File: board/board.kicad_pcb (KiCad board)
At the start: 2 copper layers, 28.4 x 40.1 mm, 36 parts, among them J1 Conn_01x02, J101 Conn_01x06, J102 Conn_01x06, J2 Conn_01x02, J3 Conn_01x06, K1 G6K-2, K2 G6K-2, Q1 IRLB8721PBF, Q2 AO3400A, Q3 IRLB8721PBF, Q4 AO3400A, U1 ATmega8A-AU, U101 ATmega128A-AU, X101 Crystal

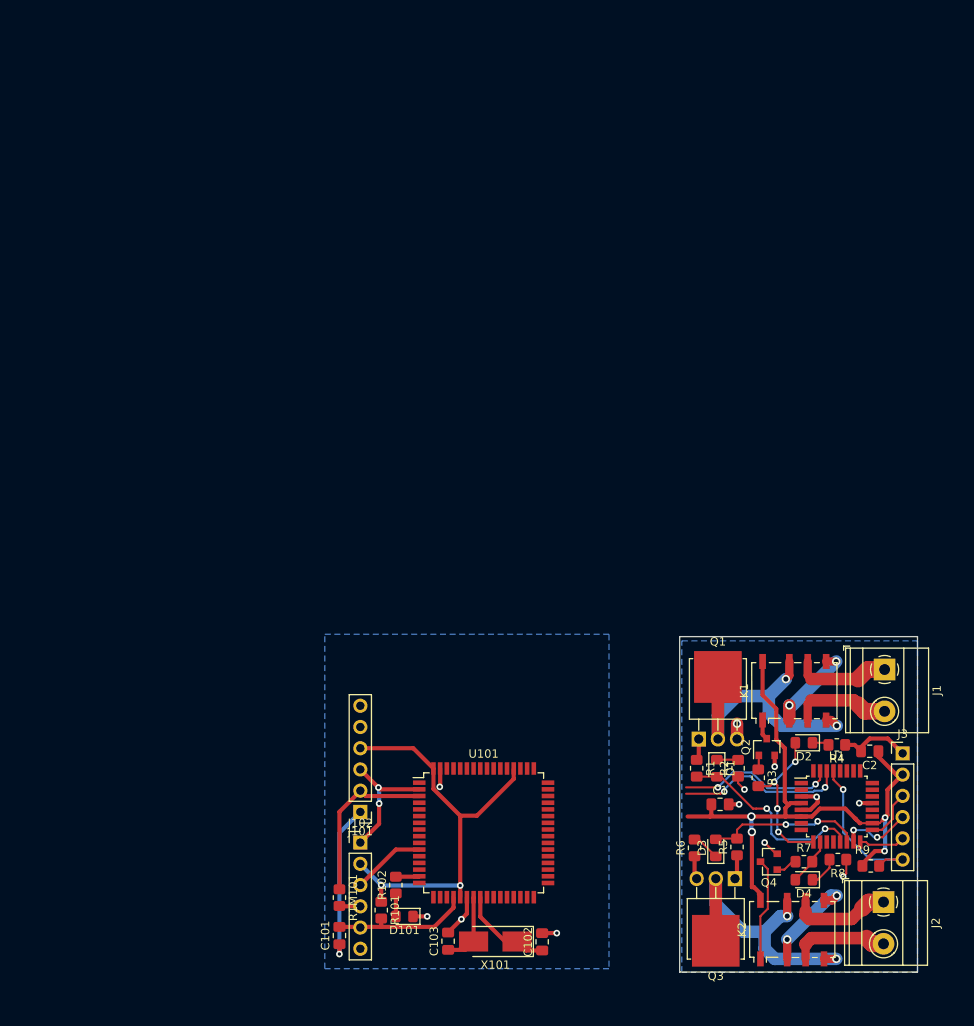
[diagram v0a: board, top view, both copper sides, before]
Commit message: uploaded updated pcb design
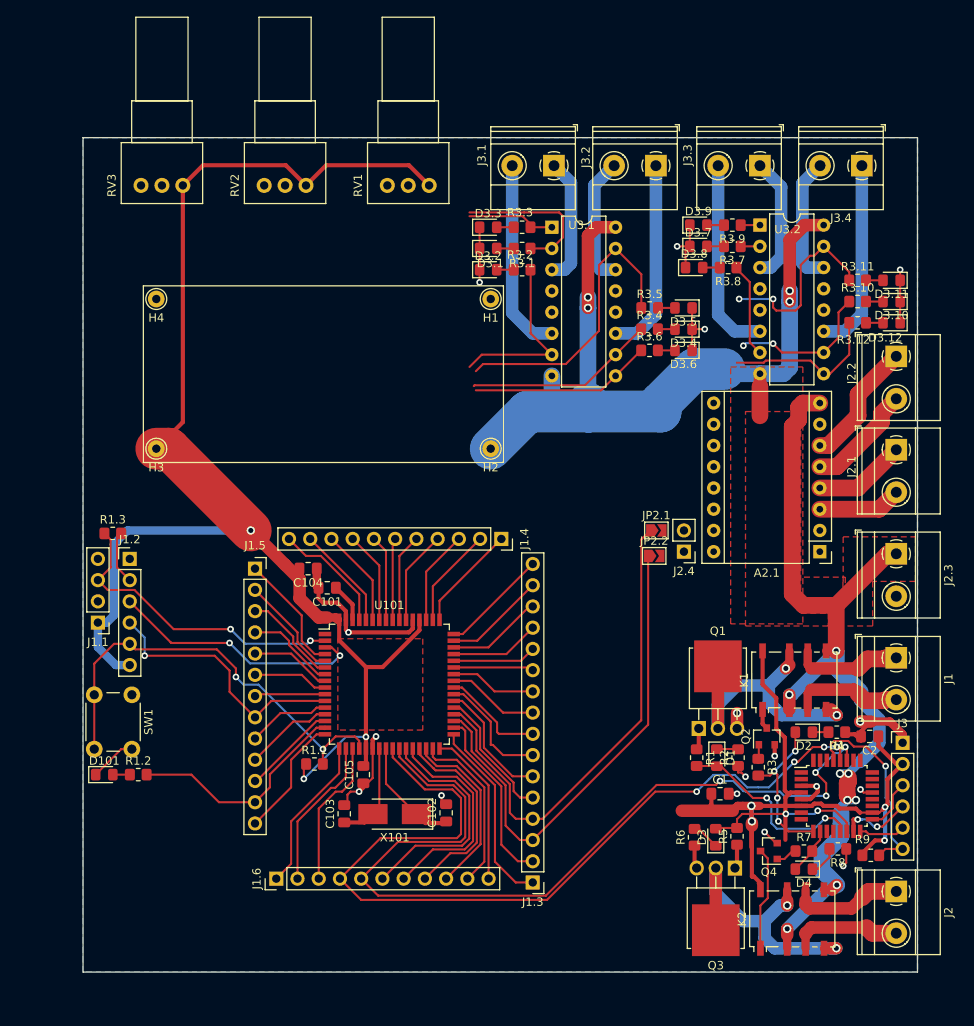
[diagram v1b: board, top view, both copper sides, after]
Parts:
- removed J101, J102: Conn_01x06, Connector_PinHeader_2.54mm:PinHeader_1x06_P2.54mm_Vertical
- removed R101, R102, R1M101: R, Resistor_SMD:R_0805_2012Metric_Pad1.20x1.40mm_HandSolder
- added A2.1: Pololu_Breakout_DRV8825, Module:Pololu_Breakout-16_15.2x20.3mm, F.Cu at (188.5, 86.9)
- added C104: C, Capacitor_SMD:C_0805_2012Metric_Pad1.18x1.45mm_HandSolder, F.Cu at (127.3, 88.9)
- added C105: C, Capacitor_SMD:C_0805_2012Metric_Pad1.18x1.45mm_HandSolder, F.Cu at (133.9, 113.5)
- added D3.1: LED, LED_SMD:LED_0805_2012Metric_Pad1.15x1.40mm_HandSolder, F.Cu at (148.8, 50.6)
- added D3.10: LED, LED_SMD:LED_0805_2012Metric_Pad1.15x1.40mm_HandSolder, F.Cu at (197.1, 56.9)
- added D3.11: LED, LED_SMD:LED_0805_2012Metric_Pad1.15x1.40mm_HandSolder, F.Cu at (197.1, 54.4)
- added D3.12: LED, LED_SMD:LED_0805_2012Metric_Pad1.15x1.40mm_HandSolder, F.Cu at (197.1, 59.5)
- added D3.2: LED, LED_SMD:LED_0805_2012Metric_Pad1.15x1.40mm_HandSolder, F.Cu at (148.8, 53.1)
- added D3.3: LED, LED_SMD:LED_0805_2012Metric_Pad1.15x1.40mm_HandSolder, F.Cu at (148.8, 48.1)
- added D3.4: LED, LED_SMD:LED_0805_2012Metric_Pad1.15x1.40mm_HandSolder, F.Cu at (172.2, 60.2)
- added D3.5: LED, LED_SMD:LED_0805_2012Metric_Pad1.15x1.40mm_HandSolder, F.Cu at (172.2, 57.7)
- added D3.6: LED, LED_SMD:LED_0805_2012Metric_Pad1.15x1.40mm_HandSolder, F.Cu at (172.2, 62.8)
- added D3.7: LED, LED_SMD:LED_0805_2012Metric_Pad1.15x1.40mm_HandSolder, F.Cu at (173.9, 50.3)
- added D3.8: LED, LED_SMD:LED_0805_2012Metric_Pad1.15x1.40mm_HandSolder, F.Cu at (173.4, 52.9)
- added D3.9: LED, LED_SMD:LED_0805_2012Metric_Pad1.15x1.40mm_HandSolder, F.Cu at (173.9, 47.8)
- added H1: GND, Connector_Pin:Pin_D1.0mm_L10.0mm, F.Cu at (149.1, 56.6)
- added H2: IN+, Connector_Pin:Pin_D1.0mm_L10.0mm, F.Cu at (149.1, 74.5)
- added H3: OUT+, Connector_Pin:Pin_D1.0mm_L10.0mm, F.Cu at (109.1, 74.5)
- added H4: GND, Connector_Pin:Pin_D1.0mm_L10.0mm, F.Cu at (109.1, 56.6)
- added J1.1: Conn_01x04, Connector_PinHeader_2.54mm:PinHeader_1x04_P2.54mm_Vertical, F.Cu at (102.1, 95.4)
- added J1.2: Conn_01x06, Connector_PinHeader_2.54mm:PinHeader_1x06_P2.54mm_Vertical, F.Cu at (105.9, 87.7)
- added J1.3: Conn_01x16, Connector_PinHeader_2.54mm:PinHeader_1x16_P2.54mm_Vertical, F.Cu at (154.1, 126.4)
- added J1.4: Conn_01x11, Connector_PinSocket_2.54mm:PinSocket_1x11_P2.54mm_Vertical, F.Cu at (150.4, 85.3)
- added J1.5: Conn_01x13, Connector_PinSocket_2.54mm:PinSocket_1x13_P2.54mm_Vertical, F.Cu at (120.9, 88.9)
- added J1.6: Conn_01x11, Connector_PinHeader_2.54mm:PinHeader_1x11_P2.54mm_Vertical, F.Cu at (123.4, 126.0)
- added J2.1: Conn_01x02, TerminalBlock_Phoenix:TerminalBlock_Phoenix_MKDS-1,5-2-5.08_1x02_P5.08mm_Horizontal, F.Cu at (197.6, 74.7)
- added J2.2: Conn_01x02, TerminalBlock_Phoenix:TerminalBlock_Phoenix_MKDS-1,5-2-5.08_1x02_P5.08mm_Horizontal, F.Cu at (197.6, 63.5)
- added J2.3: Conn_01x02, TerminalBlock_Phoenix:TerminalBlock_Phoenix_MKDS-1,5-2-5.08_1x02_P5.08mm_Horizontal, F.Cu at (197.6, 87.1)
- added J2.4: Conn_01x02, Connector_PinHeader_2.54mm:PinHeader_1x02_P2.54mm_Vertical, F.Cu at (172.2, 86.9)
- added J3.1: Conn_01x02, TerminalBlock_Phoenix:TerminalBlock_Phoenix_MKDS-1,5-2_1x02_P5.00mm_Horizontal, F.Cu at (156.7, 40.7)
- added J3.2: Conn_01x02, TerminalBlock_Phoenix:TerminalBlock_Phoenix_MKDS-1,5-2_1x02_P5.00mm_Horizontal, F.Cu at (168.9, 40.7)
- added J3.3: Conn_01x02, TerminalBlock_Phoenix:TerminalBlock_Phoenix_MKDS-1,5-2_1x02_P5.00mm_Horizontal, F.Cu at (181.3, 40.7)
- added J3.4: Conn_01x02, TerminalBlock_Phoenix:TerminalBlock_Phoenix_MKDS-1,5-2_1x02_P5.00mm_Horizontal, F.Cu at (193.5, 40.7)
- added JP2.1: Jumper_2_Open, Jumper:SolderJumper-2_P1.3mm_Open_TrianglePad1.0x1.5mm, F.Cu at (168.9, 84.3)
- added JP2.2: Jumper_2_Open, Jumper:SolderJumper-2_P1.3mm_Open_TrianglePad1.0x1.5mm, F.Cu at (168.7, 87.4)
- added R1.1: R, Resistor_SMD:R_0805_2012Metric_Pad1.20x1.40mm_HandSolder, F.Cu at (128.0, 112.3)
- added R1.2: R, Resistor_SMD:R_0805_2012Metric_Pad1.20x1.40mm_HandSolder, F.Cu at (106.9, 113.5)
- added R1.3: R, Resistor_SMD:R_0805_2012Metric_Pad1.20x1.40mm_HandSolder, F.Cu at (103.9, 84.7)
- added R3.1: 200, Resistor_SMD:R_0805_2012Metric_Pad1.20x1.40mm_HandSolder, F.Cu at (152.9, 50.6)
- added R3.10: 200, Resistor_SMD:R_0805_2012Metric_Pad1.20x1.40mm_HandSolder, F.Cu at (193.0, 56.9)
- added R3.11: 200, Resistor_SMD:R_0805_2012Metric_Pad1.20x1.40mm_HandSolder, F.Cu at (193.0, 54.4)
- added R3.12: 200, Resistor_SMD:R_0805_2012Metric_Pad1.20x1.40mm_HandSolder, F.Cu at (193.0, 59.5)
- added R3.2: 200, Resistor_SMD:R_0805_2012Metric_Pad1.20x1.40mm_HandSolder, F.Cu at (152.9, 53.1)
- added R3.3: 200, Resistor_SMD:R_0805_2012Metric_Pad1.20x1.40mm_HandSolder, F.Cu at (152.9, 48.1)
- added R3.4: 200, Resistor_SMD:R_0805_2012Metric_Pad1.20x1.40mm_HandSolder, F.Cu at (168.1, 60.2)
- added R3.5: 200, Resistor_SMD:R_0805_2012Metric_Pad1.20x1.40mm_HandSolder, F.Cu at (168.1, 57.7)
- added R3.6: 200, Resistor_SMD:R_0805_2012Metric_Pad1.20x1.40mm_HandSolder, F.Cu at (168.1, 62.8)
- added R3.7: 200, Resistor_SMD:R_0805_2012Metric_Pad1.20x1.40mm_HandSolder, F.Cu at (178.0, 50.3)
- added R3.8: 200, Resistor_SMD:R_0805_2012Metric_Pad1.20x1.40mm_HandSolder, F.Cu at (177.5, 52.9)
- added R3.9: 200, Resistor_SMD:R_0805_2012Metric_Pad1.20x1.40mm_HandSolder, F.Cu at (178.0, 47.8)
- added RV1: R_POT, Potentiometer_THT:Potentiometer_Alps_RK097_Single_Horizontal, F.Cu at (141.7, 43.1)
- added RV2: R_POT, Potentiometer_THT:Potentiometer_Alps_RK097_Single_Horizontal, F.Cu at (127.0, 43.1)
- added RV3: R_POT, Potentiometer_THT:Potentiometer_Alps_RK097_Single_Horizontal, F.Cu at (112.3, 43.1)
- added SW1: SW_Push, Button_Switch_THT:SW_PUSH_6mm_H4.3mm, F.Cu at (106.2, 104.0)
- added U3.1: L293D, Package_DIP:DIP-16_W7.62mm, F.Cu at (156.4, 48.1)
- added U3.2: L293D, Package_DIP:DIP-16_W7.62mm, F.Cu at (181.3, 47.8)
- moved C101 41.6 mm to (129.5, 91.2), turned to 180 degrees
- moved D101 39.7 mm to (102.9, 113.5), turned to 0 degrees
- moved U101 21.1 mm to (137.0, 102.7)
- moved C103 19.7 mm to (131.6, 118.2)
- moved X101 19.4 mm to (137.6, 118.3)
- moved C102 19.2 mm to (143.8, 118.1)
- moved J2 1.98 mm to (197.6, 127.5)
- moved J1 1.98 mm to (197.6, 99.6)
- moved C2 1.78 mm to (194.4, 109.0)
- moved R4 1.52 mm to (190.5, 108.5)
- moved D4 1.27 mm to (186.6, 124.8)
- moved J3 1.27 mm to (198.4, 109.7)
- moved K2 1.27 mm to (185.2, 130.8)
- moved Q1 1.27 mm to (174.0, 108.0)
- moved Q2 1.27 mm to (182.1, 109.0)
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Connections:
- net /RX renamed Net-(U1-Pad30)
- net /TX renamed Net-(U1-Pad31)
- net /V_MOT renamed V_MOT
- C1 pad 1: /5V -> 5V
- C101 pad 1: /Sheet5F90A712/DTR -> Net-(C101-Pad1)
- C101 pad 2: /Sheet5F90A712/RESET -> GND
- C2 pad 1: /5V -> 5V
- J3 pad 2: /5V -> 5V
- K1 pad 8: /5V -> 5V
- K2 pad 8: /5V -> 5V
- R9 pad 2: /5V -> 5V
- U1 pad 18: /5V -> 5V
- U1 pad 27: Net-(U1-Pad27) -> PD1
- U1 pad 28: Net-(U1-Pad28) -> PD0
- U1 pad 4: /5V -> 5V
- U1 pad 6: /5V -> 5V
- U101 pad 10: Net-(U101-Pad10) -> PB0
- U101 pad 11: /Sheet5F90A712/SCK -> PB1
- U101 pad 12: Net-(U101-Pad12) -> PB2
- U101 pad 13: Net-(U101-Pad13) -> PB3
- U101 pad 14: Net-(U101-Pad14) -> PB4
- U101 pad 15: Net-(R102-Pad2) -> PB5
- U101 pad 16: Net-(U101-Pad16) -> PB6
- U101 pad 17: Net-(U101-Pad17) -> PB7
- U101 pad 18: Net-(U101-Pad18) -> PG3
- U101 pad 19: Net-(U101-Pad19) -> PG4
- U101 pad 2: /Sheet5F90A712/TX -> /atmega128/TX
- U101 pad 20: /Sheet5F90A712/RESET -> /atmega128/RESET
- U101 pad 21: VCC -> 5V
- U101 pad 25: Net-(U101-Pad25) -> PD0
- U101 pad 26: Net-(U101-Pad26) -> PD1
- U101 pad 27: Net-(U101-Pad27) -> PD2
- U101 pad 28: Net-(U101-Pad28) -> PD3
- U101 pad 29: Net-(U101-Pad29) -> PD4
- U101 pad 3: /Sheet5F90A712/RX -> /atmega128/PDO
- U101 pad 30: Net-(U101-Pad30) -> PD5
- U101 pad 31: Net-(U101-Pad31) -> PD6
- U101 pad 32: Net-(U101-Pad32) -> PD7
- U101 pad 33: Net-(U101-Pad33) -> PG0
- U101 pad 34: Net-(U101-Pad34) -> PG1
- U101 pad 35: Net-(U101-Pad35) -> PC0
- U101 pad 36: Net-(U101-Pad36) -> PC1
- U101 pad 37: Net-(U101-Pad37) -> PC2
- U101 pad 38: Net-(U101-Pad38) -> PC3
- U101 pad 39: Net-(U101-Pad39) -> PC4
- U101 pad 4: Net-(U101-Pad4) -> PE2
- U101 pad 40: Net-(U101-Pad40) -> PC5
- U101 pad 41: Net-(U101-Pad41) -> PC6
- U101 pad 42: Net-(U101-Pad42) -> PC7
- U101 pad 43: Net-(U101-Pad43) -> PG2
- U101 pad 44: Net-(U101-Pad44) -> PA7
- U101 pad 45: Net-(U101-Pad45) -> PA6
- U101 pad 46: Net-(U101-Pad46) -> PA5
- U101 pad 47: Net-(U101-Pad47) -> PA4
- U101 pad 48: Net-(U101-Pad48) -> PA3
- U101 pad 49: Net-(U101-Pad49) -> PA2
- U101 pad 5: Net-(U101-Pad5) -> M1PWM
- U101 pad 50: Net-(U101-Pad50) -> PA1
- U101 pad 51: Net-(U101-Pad51) -> PA0
- U101 pad 52: VCC -> 5V
- U101 pad 54: Net-(U101-Pad54) -> PF7
- U101 pad 55: Net-(U101-Pad55) -> PF6
- U101 pad 56: Net-(U101-Pad56) -> PF5
- U101 pad 57: Net-(U101-Pad57) -> PF4
- U101 pad 58: Net-(U101-Pad58) -> PF3
- U101 pad 59: Net-(U101-Pad59) -> PF2
- U101 pad 6: Net-(U101-Pad6) -> PE4
- U101 pad 60: Net-(U101-Pad60) -> PF1
- U101 pad 61: Net-(U101-Pad61) -> PF0
- U101 pad 62: Net-(U101-Pad62) -> Net-(C101-Pad1)
- U101 pad 64: VCC -> 5V
- U101 pad 7: Net-(U101-Pad7) -> PE5
- U101 pad 8: Net-(U101-Pad8) -> PE6
- U101 pad 9: Net-(U101-Pad9) -> PE7
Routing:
- net 5V: track 0.00 -> 260.5 mm, vias 0 -> 7
- net V_MOT: track 22.9 -> 199.5 mm, vias 4 -> 12
- net PD0: track 0.00 -> 103.6 mm, vias 0 -> 4
- net PD1: track 0.00 -> 103.1 mm, vias 0 -> 4
- net /5V: track 77.6 -> 0.00 mm, vias 4 -> 0
- net PC0: track 0.00 -> 59.2 mm
- net PC1: track 0.00 -> 59.1 mm
- net GND: track 39.8 -> 95.4 mm, vias 12 -> 17
- net /atmega128/RESET: track 0.00 -> 52.3 mm, vias 0 -> 2
- net VCC: track 51.0 -> 0.00 mm, vias 2 -> 0
- net /atmega128/TX: track 0.00 -> 37.2 mm, vias 0 -> 2
- net M2B: track 0.00 -> 35.8 mm
- net PB1: track 0.00 -> 31.6 mm, vias 0 -> 1
- net /atmega128/PDO: track 0.00 -> 30.8 mm, vias 0 -> 2
- net PD2: track 0.00 -> 28.1 mm
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- added copper zone on F.Cu, net 5V
- added copper zone on F.Cu, net V_MOT
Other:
- board size 28.4 x 40.1 mm -> 99.8 x 99.8 mm

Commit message: updated pcb design
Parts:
- added D1.2: LED, LED_SMD:LED_0805_2012Metric_Pad1.15x1.40mm_HandSolder, F.Cu at (110.7, 90.2)
- added D1.3: LED, LED_SMD:LED_0805_2012Metric_Pad1.15x1.40mm_HandSolder, F.Cu at (110.5, 94.0)
- added D1.4: LED, LED_SMD:LED_0805_2012Metric_Pad1.15x1.40mm_HandSolder, F.Cu at (110.6, 98.1)
- added D1.5: LED, LED_SMD:LED_0805_2012Metric_Pad1.15x1.40mm_HandSolder, F.Cu at (110.5, 102.4)
- added H5: MountingHole, MountingHole:MountingHole_2.5mm_Pad, F.Cu at (103.8, 50.4)
- added H6: MountingHole, MountingHole:MountingHole_2.5mm_Pad, F.Cu at (103.7, 125.7)
- added H7: MountingHole, MountingHole:MountingHole_2.5mm_Pad, F.Cu at (168.3, 76.3)
- added J1.11: EN, TestPoint:TestPoint_THTPad_1.0x1.0mm_Drill0.5mm, F.Cu at (156.2, 117.8)
- added J1.12: ALED, TestPoint:TestPoint_THTPad_1.0x1.0mm_Drill0.5mm, F.Cu at (156.2, 119.3)
- added J1.13: STAT, TestPoint:TestPoint_THTPad_1.0x1.0mm_Drill0.5mm, F.Cu at (156.2, 120.8)
- added J1.14: SELECT, TestPoint:TestPoint_THTPad_1.0x1.0mm_Drill0.5mm, F.Cu at (156.2, 122.3)
- added J1.15: , TestPoint:TestPoint_THTPad_1.0x1.0mm_Drill0.5mm, F.Cu at (156.2, 123.8)
- added J1.16: , TestPoint:TestPoint_THTPad_1.0x1.0mm_Drill0.5mm, F.Cu at (156.2, 125.3)
- added J1.17: , TestPoint:TestPoint_THTPad_1.0x1.0mm_Drill0.5mm, F.Cu at (156.2, 126.8)
- added J1.18: , TestPoint:TestPoint_THTPad_1.0x1.0mm_Drill0.5mm, F.Cu at (156.2, 128.3)
- added J1.19: , TestPoint:TestPoint_THTPad_1.0x1.0mm_Drill0.5mm, F.Cu at (156.2, 129.8)
- added J1.20: , TestPoint:TestPoint_THTPad_1.0x1.0mm_Drill0.5mm, F.Cu at (156.2, 131.3)
- added J1.21: , TestPoint:TestPoint_THTPad_1.0x1.0mm_Drill0.5mm, F.Cu at (156.2, 132.8)
- added J1.22: , TestPoint:TestPoint_THTPad_1.0x1.0mm_Drill0.5mm, F.Cu at (156.2, 134.3)
- added J1.23: GND, TestPoint:TestPoint_THTPad_1.0x1.0mm_Drill0.5mm, F.Cu at (169.9, 116.2)
- added J1.24: VCC, TestPoint:TestPoint_THTPad_1.0x1.0mm_Drill0.5mm, F.Cu at (169.9, 117.7)
- added J1.25: RST, TestPoint:TestPoint_THTPad_1.0x1.0mm_Drill0.5mm, F.Cu at (169.9, 119.2)
- added J1.26: , TestPoint:TestPoint_THTPad_1.0x1.0mm_Drill0.5mm, F.Cu at (169.9, 120.7)
- added J1.27: SWI, TestPoint:TestPoint_THTPad_1.0x1.0mm_Drill0.5mm, F.Cu at (169.9, 122.2)
- added J1.28: , TestPoint:TestPoint_THTPad_1.0x1.0mm_Drill0.5mm, F.Cu at (169.9, 123.7)
- added J1.29: , TestPoint:TestPoint_THTPad_1.0x1.0mm_Drill0.5mm, F.Cu at (169.9, 125.2)
- added J1.30: , TestPoint:TestPoint_THTPad_1.0x1.0mm_Drill0.5mm, F.Cu at (169.9, 126.7)
- added J1.31: , TestPoint:TestPoint_THTPad_1.0x1.0mm_Drill0.5mm, F.Cu at (169.9, 128.2)
- added J1.32: RTS, TestPoint:TestPoint_THTPad_1.0x1.0mm_Drill0.5mm, F.Cu at (169.9, 129.7)
- added J1.33: CTS, TestPoint:TestPoint_THTPad_1.0x1.0mm_Drill0.5mm, F.Cu at (169.9, 131.2)
- added J1.34: RXD, TestPoint:TestPoint_THTPad_1.0x1.0mm_Drill0.5mm, F.Cu at (169.9, 132.7)
- added J1.35: TXD, TestPoint:TestPoint_THTPad_1.0x1.0mm_Drill0.5mm, F.Cu at (169.9, 134.2)
- added J1.36: Conn_01x04, Connector_PinHeader_2.54mm:PinHeader_1x04_P2.54mm_Vertical, F.Cu at (105.8, 112.3)
- added J1.7: Conn_01x04, Connector_PinHeader_2.54mm:PinHeader_1x04_P2.54mm_Vertical, F.Cu at (115.8, 119.4)
- added J2.5: Conn_01x04, Connector_PinHeader_2.54mm:PinHeader_1x04_P2.54mm_Vertical, F.Cu at (101.8, 56.0)
- added J2.6: Conn_01x04, Connector_PinHeader_2.54mm:PinHeader_1x04_P2.54mm_Vertical, F.Cu at (104.9, 55.9)
- added J2.7: Conn_01x04, Connector_PinHeader_2.54mm:PinHeader_1x04_P2.54mm_Vertical, F.Cu at (104.8, 67.9)
- added J2.8: Conn_01x04, Connector_PinHeader_2.54mm:PinHeader_1x04_P2.54mm_Vertical, F.Cu at (101.8, 67.9)
- added J3.5: Conn_01x06, Connector_PinHeader_2.54mm:PinHeader_1x06_P2.54mm_Vertical, F.Cu at (116.5, 69.1)
- added J3.6: Conn_01x06, Connector_PinHeader_2.54mm:PinHeader_1x06_P2.54mm_Vertical, F.Cu at (132.7, 69.1)
- added J37: Conn_01x05, Connector_PinHeader_2.54mm:PinHeader_1x05_P2.54mm_Vertical, F.Cu at (168.1, 115.7)
- added JP1.1: M4PWM, Jumper:SolderJumper-2_P1.3mm_Open_TrianglePad1.0x1.5mm, F.Cu at (109.3, 120.5)
- added JP1.2: M4PWM, Jumper:SolderJumper-2_P1.3mm_Open_TrianglePad1.0x1.5mm, F.Cu at (109.4, 117.7)
- added JP1.3: M4PWM, Jumper:SolderJumper-2_P1.3mm_Open_TrianglePad1.0x1.5mm, F.Cu at (109.4, 114.8)
- added JP1.4: M4PWM, Jumper:SolderJumper-2_P1.3mm_Open_TrianglePad1.0x1.5mm, F.Cu at (109.3, 112.0)
- added JP3.10: M1B, Jumper:SolderJumper-2_P1.3mm_Open_TrianglePad1.0x1.5mm, F.Cu at (116.3, 72.2)
- added JP3.11: M4PWM, Jumper:SolderJumper-2_P1.3mm_Open_TrianglePad1.0x1.5mm, F.Cu at (145.3, 72.3)
- added JP3.12: M4A, Jumper:SolderJumper-2_P1.3mm_Open_TrianglePad1.0x1.5mm, F.Cu at (142.9, 72.3)
- added JP3.13: M4B, Jumper:SolderJumper-2_P1.3mm_Open_TrianglePad1.0x1.5mm, F.Cu at (140.2, 72.2)
- added JP3.14: M3A, Jumper:SolderJumper-2_P1.3mm_Open_TrianglePad1.0x1.5mm, F.Cu at (137.7, 72.3)
- added JP3.15: M3PWM, Jumper:SolderJumper-2_P1.3mm_Open_TrianglePad1.0x1.5mm, F.Cu at (135.1, 72.3)
- added JP3.16: M3B, Jumper:SolderJumper-2_P1.3mm_Open_TrianglePad1.0x1.5mm, F.Cu at (132.6, 72.3)
- added JP3.5: M2PWM, Jumper:SolderJumper-2_P1.3mm_Open_TrianglePad1.0x1.5mm, F.Cu at (128.9, 72.3)
- added JP3.6: M2A, Jumper:SolderJumper-2_P1.3mm_Open_TrianglePad1.0x1.5mm, F.Cu at (126.5, 72.2)
- added JP3.7: M2B, Jumper:SolderJumper-2_P1.3mm_Open_TrianglePad1.0x1.5mm, F.Cu at (124.0, 72.2)
- added JP3.8: M1PWM, Jumper:SolderJumper-2_P1.3mm_Open_TrianglePad1.0x1.5mm, F.Cu at (121.4, 72.2)
- added JP3.9: M1A, Jumper:SolderJumper-2_P1.3mm_Open_TrianglePad1.0x1.5mm, F.Cu at (118.9, 72.2)
- added Q1.1: AO3400A, Package_TO_SOT_SMD:SOT-23, F.Cu at (166.1, 111.6)
- added R1.10: R, Resistor_SMD:R_0805_2012Metric_Pad1.20x1.40mm_HandSolder, F.Cu at (160.0, 124.2)
- added R1.11: R, Resistor_SMD:R_0805_2012Metric_Pad1.20x1.40mm_HandSolder, F.Cu at (163.9, 124.2)
- added R1.12: R, Resistor_SMD:R_0805_2012Metric_Pad1.20x1.40mm_HandSolder, F.Cu at (162.0, 112.5)
- added R1.13: R, Resistor_SMD:R_0805_2012Metric_Pad1.20x1.40mm_HandSolder, F.Cu at (119.9, 130.6)
- added R1.14: R, Resistor_SMD:R_0805_2012Metric_Pad1.20x1.40mm_HandSolder, F.Cu at (119.9, 132.8)
- added R1.4: R, Resistor_SMD:R_0805_2012Metric_Pad1.20x1.40mm_HandSolder, F.Cu at (113.6, 91.0)
- added R1.5: R, Resistor_SMD:R_0805_2012Metric_Pad1.20x1.40mm_HandSolder, F.Cu at (113.5, 94.9)
- added R1.6: R, Resistor_SMD:R_0805_2012Metric_Pad1.20x1.40mm_HandSolder, F.Cu at (113.5, 98.9)
- added R1.7: R, Resistor_SMD:R_0805_2012Metric_Pad1.20x1.40mm_HandSolder, F.Cu at (113.4, 102.9)
- added R1.8: R, Resistor_SMD:R_0805_2012Metric_Pad1.20x1.40mm_HandSolder, F.Cu at (166.1, 108.4)
- added R1.9: R, Resistor_SMD:R_0805_2012Metric_Pad1.20x1.40mm_HandSolder, F.Cu at (162.0, 110.1)
- added SW1.2: SW_Push, Button_Switch_THT:SW_PUSH_6mm_H4.3mm, F.Cu at (123.7, 130.5)
- added SW1.3: SW_Push, Button_Switch_THT:SW_PUSH_6mm_H4.3mm, F.Cu at (134.1, 130.5)
- added TP1: TestPoint, TestPoint:TestPoint_Pad_4.0x4.0mm, F.Cu at (169.3, 91.4)
- added TP10: TestPoint, TestPoint:TestPoint_Pad_4.0x4.0mm, B.Cu at (143.0, 58.5)
- added TP100: TestPoint, TestPoint:TestPoint_Pad_4.0x4.0mm, F.Cu at (110.3, 125.3)
- added TP101: TestPoint, TestPoint:TestPoint_Pad_4.0x4.0mm, F.Cu at (108.3, 134.1)
- added TP102: TestPoint, TestPoint:TestPoint_Pad_4.0x4.0mm, F.Cu at (110.3, 129.7)
- added TP11: TestPoint, TestPoint:TestPoint_Pad_4.0x4.0mm, B.Cu at (138.6, 58.5)
- added TP12: TestPoint, TestPoint:TestPoint_Pad_4.0x4.0mm, F.Cu at (164.5, 95.8)
- added TP13: TestPoint, TestPoint:TestPoint_Pad_4.0x4.0mm, B.Cu at (123.1, 54.1)
- added TP14: TestPoint, TestPoint:TestPoint_Pad_4.0x4.0mm, B.Cu at (140.7, 54.1)
- added TP15: TestPoint, TestPoint:TestPoint_Pad_4.0x4.0mm, B.Cu at (140.7, 62.9)
- added TP16: TestPoint, TestPoint:TestPoint_Pad_4.0x4.0mm, B.Cu at (134.2, 58.5)
- added TP17: TestPoint, TestPoint:TestPoint_Pad_4.0x4.0mm, B.Cu at (136.3, 54.1)
- added TP18: TestPoint, TestPoint:TestPoint_Pad_4.0x4.0mm, F.Cu at (160.0, 128.8)
- added TP19: TestPoint, TestPoint:TestPoint_Pad_4.0x4.0mm, B.Cu at (143.0, 49.7)
- added TP2: TestPoint, TestPoint:TestPoint_Pad_4.0x4.0mm, F.Cu at (163.2, 91.4)
- added TP20: TestPoint, TestPoint:TestPoint_Pad_4.0x4.0mm, B.Cu at (136.3, 62.9)
- added TP21: TestPoint, TestPoint:TestPoint_Pad_4.0x4.0mm, B.Cu at (169.2, 91.4)
- added TP22: TestPoint, TestPoint:TestPoint_Pad_4.0x4.0mm, B.Cu at (129.8, 58.5)
- added TP23: TestPoint, TestPoint:TestPoint_Pad_4.0x4.0mm, B.Cu at (131.9, 54.1)
- added TP24: TestPoint, TestPoint:TestPoint_Pad_4.0x4.0mm, B.Cu at (138.6, 49.7)
- added TP25: TestPoint, TestPoint:TestPoint_Pad_4.0x4.0mm, F.Cu at (160.1, 104.6)
- added TP26: TestPoint, TestPoint:TestPoint_Pad_4.0x4.0mm, B.Cu at (131.9, 62.9)
- added TP27: TestPoint, TestPoint:TestPoint_Pad_4.0x4.0mm, B.Cu at (163.2, 91.4)
- added TP28: TestPoint, TestPoint:TestPoint_Pad_4.0x4.0mm, B.Cu at (162.1, 109.0)
- added TP29: TestPoint, TestPoint:TestPoint_Pad_4.0x4.0mm, B.Cu at (125.4, 58.5)
- added TP3: TestPoint, TestPoint:TestPoint_Pad_4.0x4.0mm, F.Cu at (168.9, 104.6)
- added TP30: TestPoint, TestPoint:TestPoint_Pad_4.0x4.0mm, B.Cu at (127.5, 54.1)
- added TP31: TestPoint, TestPoint:TestPoint_Pad_4.0x4.0mm, B.Cu at (134.2, 49.7)
- added TP32: TestPoint, TestPoint:TestPoint_Pad_4.0x4.0mm, F.Cu at (116.3, 80.8)
- added TP33: TestPoint, TestPoint:TestPoint_Pad_4.0x4.0mm, B.Cu at (127.5, 62.9)
- added TP34: TestPoint, TestPoint:TestPoint_Pad_4.0x4.0mm, B.Cu at (150.9, 133.8)
- added TP35: TestPoint, TestPoint:TestPoint_Pad_4.0x4.0mm, B.Cu at (166.5, 109.0)
- added TP36: TestPoint, TestPoint:TestPoint_Pad_4.0x4.0mm, B.Cu at (168.9, 104.6)
- added TP37: TestPoint, TestPoint:TestPoint_Pad_4.0x4.0mm, F.Cu at (160.1, 95.8)
- added TP38: TestPoint, TestPoint:TestPoint_Pad_4.0x4.0mm, B.Cu at (129.8, 49.7)
- added TP39: TestPoint, TestPoint:TestPoint_Pad_4.0x4.0mm, B.Cu at (116.6, 49.7)
- added TP4: TestPoint, TestPoint:TestPoint_Pad_4.0x4.0mm, F.Cu at (160.0, 133.2)
- added TP40: TestPoint, TestPoint:TestPoint_Pad_4.0x4.0mm, B.Cu at (123.1, 62.9)
- added TP41: TestPoint, TestPoint:TestPoint_Pad_4.0x4.0mm, B.Cu at (176.2, 92.9)
- added TP42: TestPoint, TestPoint:TestPoint_Pad_4.0x4.0mm, F.Cu at (116.6, 58.5)
- added TP43: TestPoint, TestPoint:TestPoint_Pad_4.0x4.0mm, B.Cu at (164.5, 104.6)
- added TP44: TestPoint, TestPoint:TestPoint_Pad_4.0x4.0mm, B.Cu at (160.1, 104.6)
- added TP45: TestPoint, TestPoint:TestPoint_Pad_4.0x4.0mm, B.Cu at (125.4, 49.7)
- added TP46: TestPoint, TestPoint:TestPoint_Pad_4.0x4.0mm, B.Cu at (121.0, 49.7)
- added TP47: TestPoint, TestPoint:TestPoint_Pad_4.0x4.0mm, B.Cu at (118.7, 62.9)
- added TP48: TestPoint, TestPoint:TestPoint_Pad_4.0x4.0mm, B.Cu at (182.8, 88.5)
- added TP49: TestPoint, TestPoint:TestPoint_Pad_4.0x4.0mm, F.Cu at (138.6, 49.7)
- added TP5: TestPoint, TestPoint:TestPoint_Pad_4.0x4.0mm, F.Cu at (164.5, 104.6)
- added TP50: TestPoint, TestPoint:TestPoint_Pad_4.0x4.0mm, F.Cu at (136.3, 54.1)
- added TP51: TestPoint, TestPoint:TestPoint_Pad_4.0x4.0mm, B.Cu at (166.8, 100.2)
- added TP52: TestPoint, TestPoint:TestPoint_Pad_4.0x4.0mm, B.Cu at (168.9, 95.8)
- added TP53: TestPoint, TestPoint:TestPoint_Pad_4.0x4.0mm, B.Cu at (118.7, 54.1)
- added TP54: TestPoint, TestPoint:TestPoint_Pad_4.0x4.0mm, B.Cu at (146.5, 133.8)
- added TP55: TestPoint, TestPoint:TestPoint_Pad_4.0x4.0mm, B.Cu at (182.8, 84.1)
- added TP56: TestPoint, TestPoint:TestPoint_Pad_4.0x4.0mm, F.Cu at (138.6, 58.5)
- added TP57: TestPoint, TestPoint:TestPoint_Pad_4.0x4.0mm, F.Cu at (140.7, 54.1)
- added TP58: TestPoint, TestPoint:TestPoint_Pad_4.0x4.0mm, F.Cu at (143.0, 49.7)
- added TP59: TestPoint, TestPoint:TestPoint_Pad_4.0x4.0mm, B.Cu at (162.4, 100.2)
- added TP6: TestPoint, TestPoint:TestPoint_Pad_4.0x4.0mm, B.Cu at (121.0, 58.5)
- added TP60: TestPoint, TestPoint:TestPoint_Pad_4.0x4.0mm, B.Cu at (164.5, 95.8)
- added TP61: TestPoint, TestPoint:TestPoint_Pad_4.0x4.0mm, B.Cu at (108.3, 134.1)
- added TP62: TestPoint, TestPoint:TestPoint_Pad_4.0x4.0mm, B.Cu at (182.8, 79.7)
- added TP63: TestPoint, TestPoint:TestPoint_Pad_4.0x4.0mm, F.Cu at (143.0, 58.5)
- added TP64: TestPoint, TestPoint:TestPoint_Pad_4.0x4.0mm, F.Cu at (121.0, 58.5)
- added TP65: TestPoint, TestPoint:TestPoint_Pad_4.0x4.0mm, F.Cu at (123.1, 54.1)
- added TP66: TestPoint, TestPoint:TestPoint_Pad_4.0x4.0mm, F.Cu at (121.0, 49.7)
- added TP67: TestPoint, TestPoint:TestPoint_Pad_4.0x4.0mm, B.Cu at (160.1, 95.8)
- added TP68: TestPoint, TestPoint:TestPoint_Pad_4.0x4.0mm, F.Cu at (146.5, 133.8)
- added TP69: TestPoint, TestPoint:TestPoint_Pad_4.0x4.0mm, B.Cu at (145.1, 62.9)
- added TP7: TestPoint, TestPoint:TestPoint_Pad_4.0x4.0mm, F.Cu at (162.4, 100.2)
- added TP70: TestPoint, TestPoint:TestPoint_Pad_4.0x4.0mm, B.Cu at (182.8, 75.2)
- added TP71: TestPoint, TestPoint:TestPoint_Pad_4.0x4.0mm, F.Cu at (129.8, 58.5)
- added TP72: TestPoint, TestPoint:TestPoint_Pad_4.0x4.0mm, F.Cu at (127.5, 54.1)
- added TP73: TestPoint, TestPoint:TestPoint_Pad_4.0x4.0mm, F.Cu at (134.2, 58.5)
- added TP74: TestPoint, TestPoint:TestPoint_Pad_4.0x4.0mm, F.Cu at (116.6, 49.7)
- added TP75: TestPoint, TestPoint:TestPoint_Pad_4.0x4.0mm, B.Cu at (160.0, 133.2)
- added TP76: TestPoint, TestPoint:TestPoint_Pad_4.0x4.0mm, F.Cu at (150.9, 133.8)
- added TP77: TestPoint, TestPoint:TestPoint_Pad_4.0x4.0mm, B.Cu at (112.7, 134.1)
- added TP78: TestPoint, TestPoint:TestPoint_Pad_4.0x4.0mm, B.Cu at (110.3, 129.7)
- added TP79: TestPoint, TestPoint:TestPoint_Pad_4.0x4.0mm, F.Cu at (131.9, 54.1)
- added TP8: TestPoint, TestPoint:TestPoint_Pad_4.0x4.0mm, F.Cu at (166.8, 100.2)
- added TP80: TestPoint, TestPoint:TestPoint_Pad_4.0x4.0mm, F.Cu at (125.4, 58.5)
- added TP81: TestPoint, TestPoint:TestPoint_Pad_4.0x4.0mm, F.Cu at (125.4, 49.7)
- added TP82: TestPoint, TestPoint:TestPoint_Pad_4.0x4.0mm, B.Cu at (160.0, 128.8)
- added TP83: TestPoint, TestPoint:TestPoint_Pad_4.0x4.0mm, B.Cu at (164.4, 133.2)
- added TP84: TestPoint, TestPoint:TestPoint_Pad_4.0x4.0mm, F.Cu at (164.4, 128.8)
- added TP85: TestPoint, TestPoint:TestPoint_Pad_4.0x4.0mm, B.Cu at (116.6, 58.5)
- added TP86: TestPoint, TestPoint:TestPoint_Pad_4.0x4.0mm, B.Cu at (110.3, 125.3)
- added TP87: TestPoint, TestPoint:TestPoint_Pad_4.0x4.0mm, F.Cu at (118.7, 54.1)
- added TP88: TestPoint, TestPoint:TestPoint_Pad_4.0x4.0mm, F.Cu at (129.8, 49.7)
- added TP89: TestPoint, TestPoint:TestPoint_Pad_4.0x4.0mm, B.Cu at (185.0, 92.9)
- added TP9: TestPoint, TestPoint:TestPoint_Pad_4.0x4.0mm, F.Cu at (168.9, 95.8)
- added TP90: TestPoint, TestPoint:TestPoint_Pad_4.0x4.0mm, B.Cu at (164.4, 128.8)
- added TP91: TestPoint, TestPoint:TestPoint_Pad_4.0x4.0mm, F.Cu at (164.4, 133.2)
- added TP92: TestPoint, TestPoint:TestPoint_Pad_4.0x4.0mm, B.Cu at (103.9, 134.1)
- added TP93: TestPoint, TestPoint:TestPoint_Pad_4.0x4.0mm, B.Cu at (117.1, 134.1)
- added TP94: TestPoint, TestPoint:TestPoint_Pad_4.0x4.0mm, F.Cu at (134.2, 49.7)
- added TP95: TestPoint, TestPoint:TestPoint_Pad_4.0x4.0mm, B.Cu at (180.6, 92.9)
- added TP96: TestPoint, TestPoint:TestPoint_Pad_4.0x4.0mm, B.Cu at (189.4, 92.9)
- added TP97: TestPoint, TestPoint:TestPoint_Pad_4.0x4.0mm, F.Cu at (103.9, 134.1)
- added TP98: TestPoint, TestPoint:TestPoint_Pad_4.0x4.0mm, B.Cu at (182.8, 70.8)
- added TP99: TestPoint, TestPoint:TestPoint_Pad_4.0x4.0mm, F.Cu at (112.7, 134.1)
- added U99: viking, board:viking, F.Cu at (158.5, 79.9)
- moved D101 5.08 mm to (102.9, 108.5)
- moved J1.1 5.08 mm to (102.1, 90.3)
- moved J1.2 5.08 mm to (105.9, 82.7)
- moved R1.2 5.08 mm to (106.9, 108.5)
- moved R1.3 5.08 mm to (103.9, 79.6)
- moved SW1 5.08 mm to (106.2, 98.9)
- moved J1.3 1.82 mm to (152.4, 127.0)
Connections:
- net PC2 renamed B_STAT
- net PD2 renamed B_TXD
- net PD3 renamed B_RXD
- J1.3 pad 10: PC7 -> M4B
- J1.3 pad 11: PG2 -> M3A
- J1.3 pad 12: PA7 -> M3B
- J1.3 pad 13: PA6 -> M2A
- J1.3 pad 14: PA5 -> M2B
- J1.3 pad 15: PA4 -> M1A
- J1.3 pad 16: PA3 -> M1B
- J1.3 pad 9: PC6 -> M4A
- J1.5 pad 11: PB4 -> M4PWM
- J1.5 pad 3: PE4 -> M2PWM
- J1.5 pad 4: PE5 -> M3PWM
- R3.1 pad 1: M1A -> Net-(J3.5-Pad2)
- R3.10 pad 1: M4A -> Net-(J3.6-Pad5)
- R3.11 pad 1: M4B -> Net-(J3.6-Pad4)
- R3.12 pad 1: M4PWM -> Net-(J3.6-Pad6)
- R3.2 pad 1: M1B -> Net-(J3.5-Pad1)
- R3.3 pad 1: M1PWM -> Net-(J3.5-Pad3)
- R3.4 pad 1: M2A -> Net-(J3.5-Pad5)
- R3.5 pad 1: M2B -> Net-(J3.5-Pad4)
- R3.6 pad 1: M2PWM -> Net-(J3.5-Pad6)
- R3.7 pad 1: M3A -> Net-(J3.6-Pad3)
- R3.8 pad 1: M3B -> Net-(J3.6-Pad1)
- R3.9 pad 1: M3PWM -> Net-(J3.6-Pad2)
- RV1 pad 2: Net-(RV1-Pad2) -> PF2
- RV2 pad 2: Net-(RV2-Pad2) -> PF1
- RV3 pad 2: Net-(RV3-Pad2) -> PF0
- U101 pad 14: PB4 -> M4PWM
- U101 pad 41: PC6 -> M4A
- U101 pad 42: PC7 -> M4B
- U101 pad 43: PG2 -> M3A
- U101 pad 44: PA7 -> M3B
- U101 pad 45: PA6 -> M2A
- U101 pad 46: PA5 -> M2B
- U101 pad 47: PA4 -> M1A
- U101 pad 48: PA3 -> M1B
- U101 pad 6: PE4 -> M2PWM
- U101 pad 7: PE5 -> M3PWM
- U3.1 pad 1: M1PWM -> Net-(J3.5-Pad3)
- U3.1 pad 10: M2A -> Net-(J3.5-Pad5)
- U3.1 pad 15: M2B -> Net-(J3.5-Pad4)
- U3.1 pad 2: M1A -> Net-(J3.5-Pad2)
- U3.1 pad 7: M1B -> Net-(J3.5-Pad1)
- U3.1 pad 9: M2PWM -> Net-(J3.5-Pad6)
- U3.2 pad 1: M3PWM -> Net-(J3.6-Pad2)
- U3.2 pad 10: M4A -> Net-(J3.6-Pad5)
- U3.2 pad 15: M4B -> Net-(J3.6-Pad4)
- U3.2 pad 2: M3A -> Net-(J3.6-Pad3)
- U3.2 pad 7: M3B -> Net-(J3.6-Pad1)
- U3.2 pad 9: M4PWM -> Net-(J3.6-Pad6)
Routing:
- net 5V: track 260.5 -> 425.2 mm, vias 7 -> 14
- net PF2: track 11.7 -> 117.3 mm, vias 0 -> 3
- net PF1: track 12.4 -> 96.4 mm, vias 0 -> 3
- net Net-(J3.6-Pad1): track 0.00 -> 74.1 mm
- net Net-(J3.6-Pad4): track 0.00 -> 74.1 mm, vias 0 -> 2
- net Net-(J3.5-Pad4): track 0.00 -> 69.5 mm
- net Net-(J3.6-Pad2): track 0.00 -> 69.3 mm, vias 0 -> 1
- net Net-(J3.5-Pad3): track 0.00 -> 66.0 mm
- net Net-(J3.6-Pad3): track 0.00 -> 64.5 mm, vias 0 -> 1
- net Net-(J3.6-Pad5): track 0.00 -> 63.2 mm, vias 0 -> 2
- net M3A: track 2.30 -> 63.8 mm
- net Net-(J3.5-Pad2): track 0.00 -> 61.0 mm
- net PF0: track 14.2 -> 73.1 mm, vias 0 -> 3
- net Net-(J3.6-Pad6): track 0.00 -> 58.2 mm
- net Net-(J3.5-Pad1): track 0.00 -> 56.7 mm
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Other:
- board text added: "+"
- board text added: "-"
- board text added: "3.3V"
- board text added: "5V"
- board text added: "BAT+"
- board text added: "Designed by Michael Denissov"
- board text added: "GND"
- board text added: "GND BAT-"
- board text added: "RXD"
- board text added: "SCL"
- board text added: "SDA"
- board text added: "SERVO"
- board text added: "TXD"
- board text added: "VCC"
